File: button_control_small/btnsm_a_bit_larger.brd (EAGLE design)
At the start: 41.4 x 41.4 mm, 63 parts, among them IC2 MEGA8-AI, J1 AVR_SPI_PROG_3X2NS, J2 OUT-, J3 OUT+, Q1 2N2007 (SOT323), Q2 IRLML9301, Q3 IRLML9301, Q4 2N2007 (SOT323), Q5 IRLML9301, T1 BC848, T2 BC848, T3 BC848, T4 BC848, T5 BC848, U1 ACS711ELCTR-25AB-T

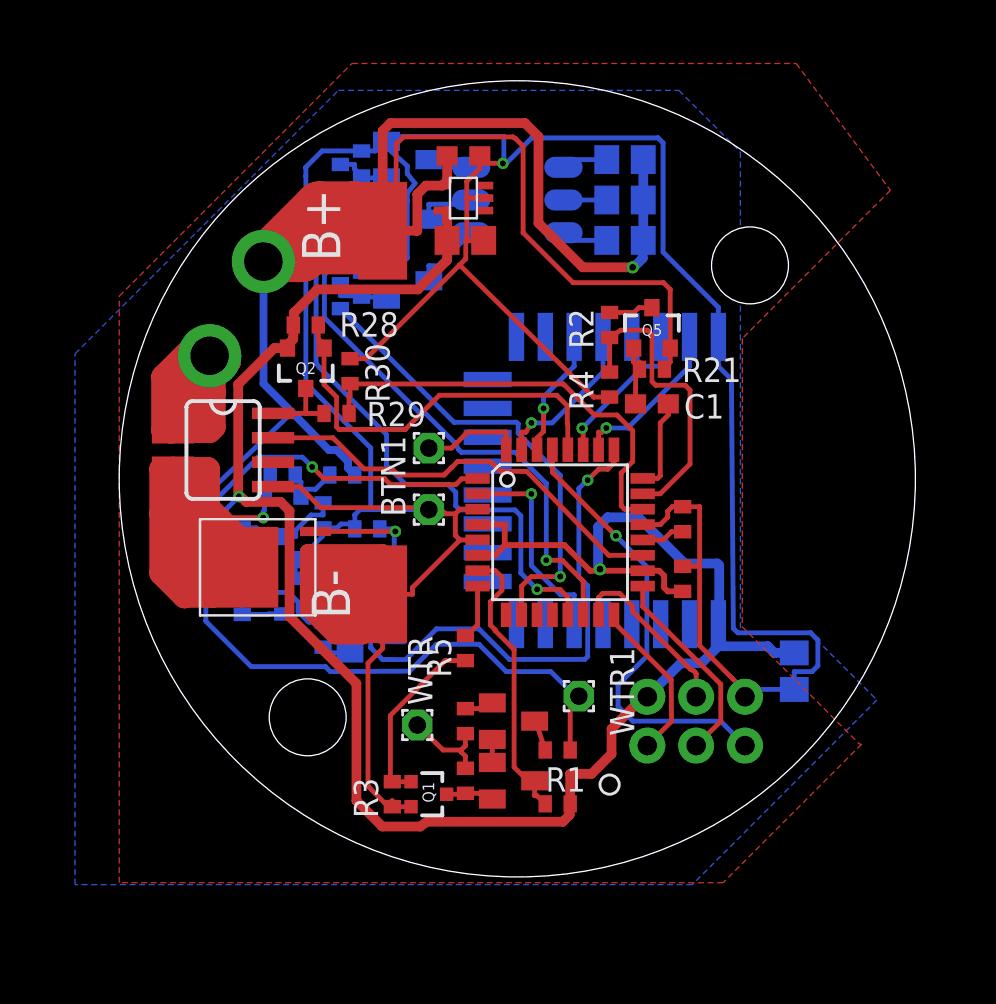
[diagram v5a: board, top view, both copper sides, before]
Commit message: Switched to HC-05
Added protection for water-input
Added separate power supply for BT & DS18B20
Added DS18B20
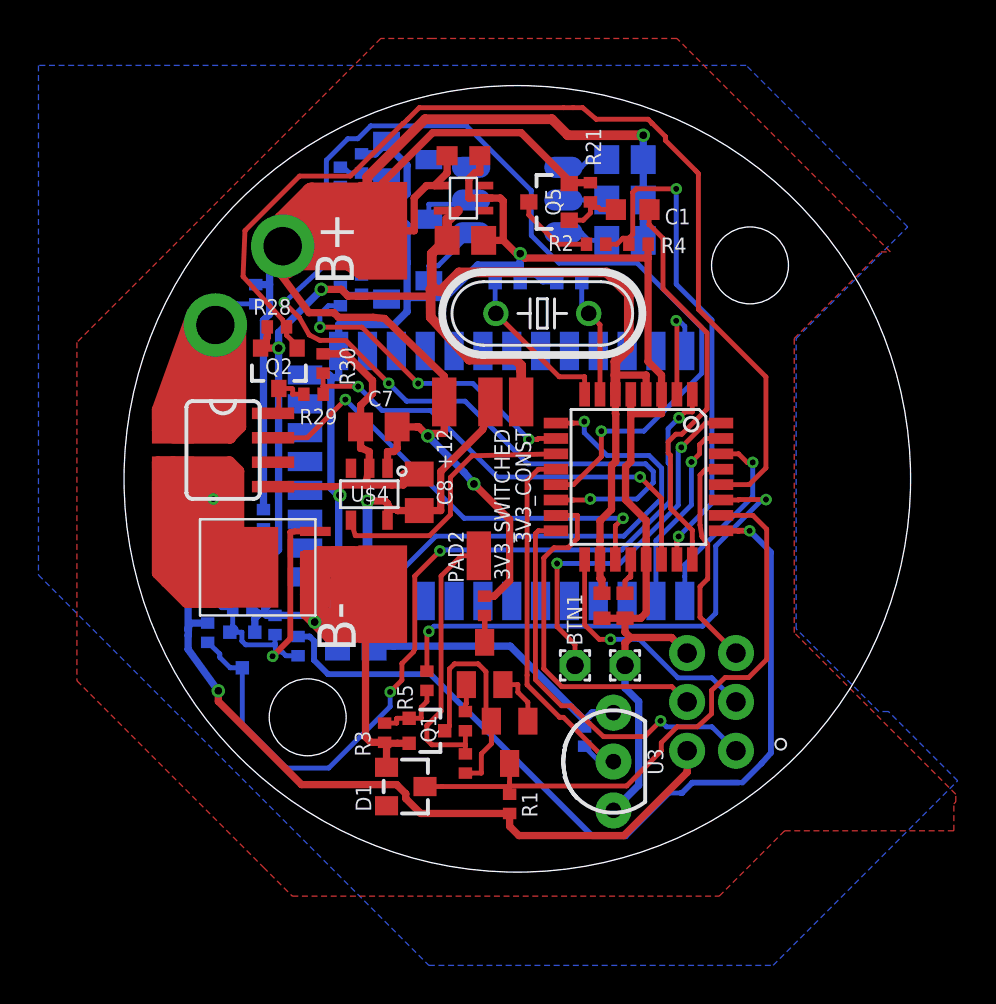
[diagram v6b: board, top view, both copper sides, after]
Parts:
- removed D3: BAT54, diode:SOT23
- removed JDY-08: JDY-08, jdy-08:JDY-08
- removed WTR: WTR-IN, wirepad:1,6/0,9
- removed WTR1: WTR-PWR, wirepad:1,6/0,9
- added +12: +12, wirepad:SMD1,27-2,54
- added 3V3_CONST: 3V_SW, wirepad:SMD1,27-2,54
- added 3V3_SWITCHED: 3V3, wirepad:SMD1,27-2,54
- added C10: 16pF, resistor:C0402
- added C7, C8: 1uF, resistor:C0805
- added C9: 10uF, resistor:C0805
- added PAD2: WTR_IN, wirepad:SMD1,27-2,54
- added Q6: 3.6864MHz, adafruit:HC49/S
- added R31: 4.7k, rcl:R0402
- added U$4: MCP1804, 1804:SOT-23-5
- added U2: HC_05, Bluetooth HC-05:BLUETOOTH_SMD
- added U3: DS18B20, SparkFun-Sensors:TO-92-AMMO
- C1: device resistor:C0603 -> resistor:C0603K
- C6: value 10uF -> 16pF; device resistor:C0805 -> resistor:C0402
- D1: value BAT54 -> BZX84CSMD; device diode:SOT23 -> diode:TO236
- Q1, Q4: value 2N2007 (SOT323) -> 310mA/60V/1.6Ω
- Q2, Q3, Q5: value IRLML9301 -> 4.3A/20V/54mΩ
- R18: value 200 -> 10k
- moved C6 23.4 mm to (22.7, 30.3), turned to 180 degrees
- moved R18 18.0 mm to (6.40, 29.6), turned to 270 degrees
- moved BTN1 13.6 mm to (23.0, 10.3)
- moved BTN2 13.0 mm to (25.6, 10.3)
- moved C1 10.1 mm to (26.0, 34.0)
- moved R21 9.74 mm to (23.8, 34.9), turned to 90 degrees
- moved Q5 8.46 mm to (21.7, 34.4), turned to 90 degrees
- moved R9 8.41 mm to (18.3, 13.4), turned to 90 degrees
- moved D1 8.10 mm to (14.2, 4.00), flipped to the top, turned to 270 degrees
- moved R4 7.45 mm to (26.3, 32.2), turned to 0 degrees
- moved R20 6.93 mm to (7.40, 12.4), turned to 90 degrees
- moved C5 5.41 mm to (25.6, 13.4), turned to 90 degrees
- moved IC2 4.99 mm to (26.3, 20.1), turned to 270 degrees
- moved R15 4.88 mm to (6.50, 14.6), turned to 180 degrees
- moved R27 4.70 mm to (6.80, 17.9), turned to 270 degrees
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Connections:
- net N$1 renamed R+
- net N$12 renamed PD3
- net N$14 renamed PC1
- net N$18 renamed WTR_MEASURE_PULLUP
- net N$21 renamed PC2
- net N$22 renamed PC0
- net N$24 renamed B-
- net N$25 renamed G-
- net N$26 renamed R-
- net N$27 renamed B-BASE
- net N$28 renamed G-BASE
- net N$29 renamed R-BASE
- net N$3 renamed B+
- net N$30 renamed PB2
- net N$31 renamed PB1
- net N$36 renamed PWR_MEASURE_VCC
- net N$5 renamed G+
- net N$6 renamed WTR_MEASURE_ON
- net N$7 renamed GND_OUT_MEASURE
- net PWM0 renamed PD6(PWM0)
- removed net N$10: Q4.1, R16.1, R18.2, R6.1
- removed net N$15: D1.1, R18.1
- removed net N$16: R10.2, R8.1, WTR.1
- removed net N$19: D3.1, R19.1
- removed net N$20: D1.3, D3.3, R20.1, U$1.4
- removed net N$33: IC2.26, JDY-08.23
- removed net N$34: J2.1, U1.1, U1.2
- removed net N$35: IC2.27, JDY-08.22
- removed net N$37: IC2.2, JDY-08.6
- removed net N$38: IC2.30, JDY-08.19
- removed net N$39: IC2.31, JDY-08.20
- new net GND_OUT: J2.1, R18.2, U1.1, U1.2
- new net OUT_BASE: Q4.1, R16.1, R19.1, R20.1, R6.1, U$1.4
- new net PB0: IC2.12, R31.1, U3.2
- new net PC3: D1.C, IC2.26, R1.1, T2.3
- new net PC4: IC2.27, R5.2
- new net PD4-HC05_KEY: IC2.2, U2.34
- new net PD5-HC05_RST: IC2.9, U2.11
- new net PD7: IC2.11, U$4.4
- new net RX(UC): IC2.30, U2.1
- new net TX(UC): IC2.31, U2.2
- new net VCC: 3V3_SWITCHED.1, C8.1, C9.1, R31.2, U$4.5, U2.12, U3.3
- new net WTR-IN: PAD2.1, R10.2, R8.1
- net +12V: now also +12.1, C7.1, R18.1, U$4.1; no longer WTR1.1
- net GND: now also C10.1, C6.1, C7.2, C8.2, C9.2, D1.A, U$4.2, U2.13, U2.21, U2.22, U3.1; no longer C6.2, JDY-08.24
- net PB6: now also C6.2, Q6.2; no longer R1.1, T2.3
- net PB7: now also C10.2, Q6.1; no longer R5.2
- net VDD: now also 3V3_CONST.1; no longer C6.1, JDY-08.1
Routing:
- net GND_OUT: track 0.00 -> 62.5 mm
- net GND_OUT_MEASURE: track 57.5 -> 100.4 mm
- net VCC: track 0.00 -> 33.9 mm, vias 0 -> 1
- net ADC5: track 21.0 -> 54.4 mm
- net PC3: track 0.00 -> 32.5 mm
- net PC4: track 0.00 -> 26.9 mm, vias 0 -> 2
- net GND: track 212.9 -> 186.8 mm, vias 1 -> 3
- net PD5-HC05_RST: track 0.00 -> 25.2 mm, vias 0 -> 1
- net N$34: track 22.6 -> 0.00 mm
- net PB0: track 0.00 -> 20.3 mm
- net PD3: track 24.3 -> 43.9 mm, vias 1 -> 3
- net OUT_BASE: track 0.00 -> 16.5 mm, vias 0 -> 1
- net PC1: track 4.89 -> 21.0 mm
- net WTR-IN: track 0.00 -> 14.5 mm
- net PD7: track 0.00 -> 14.1 mm
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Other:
- board size 41.4 x 41.4 mm -> 40.9 x 40.9 mm

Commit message: Removed extra route, slight changes to ground poly
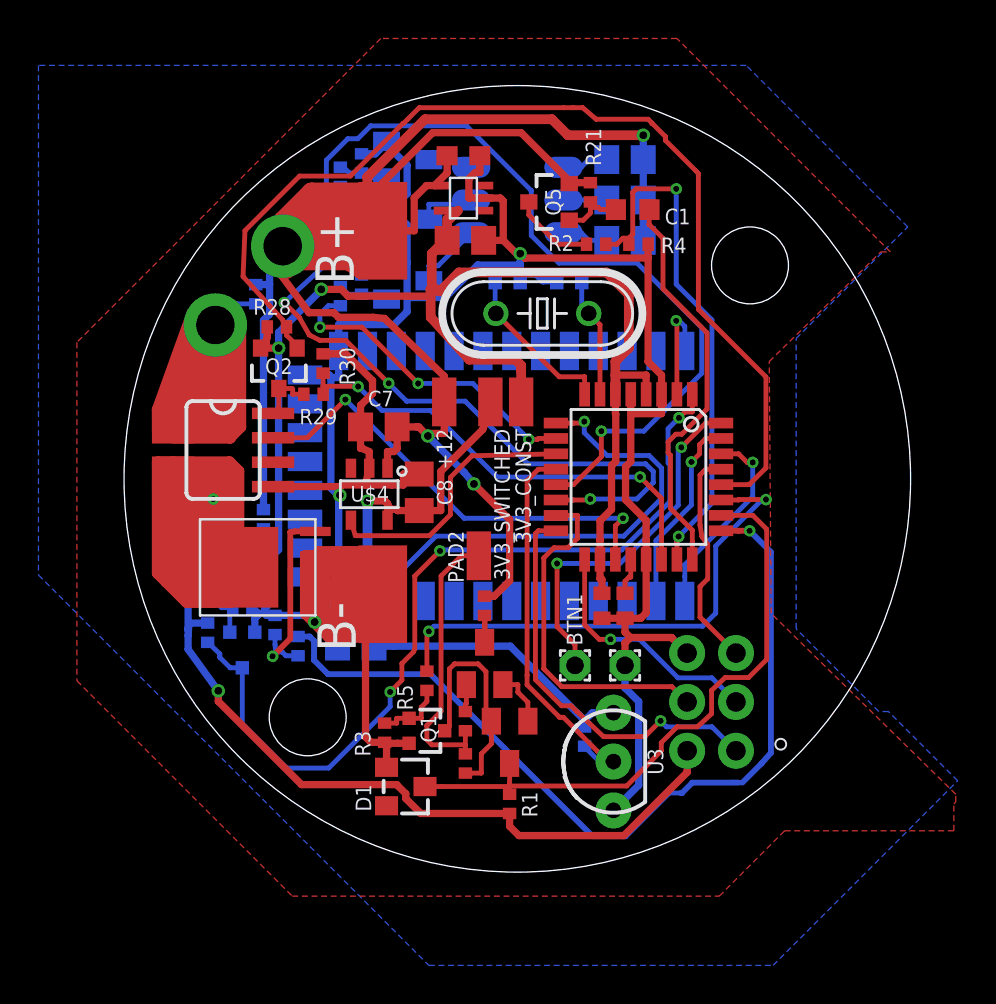
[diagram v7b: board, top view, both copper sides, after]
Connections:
- new net N$1: Q4.1, R16.1, R6.1
- net OUT_BASE: no longer Q4.1, R16.1, R6.1
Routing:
- net OUT_BASE: track 16.5 -> 10.6 mm
- net N$1: track 0.00 -> 3.04 mm
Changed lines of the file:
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@@
 <wire x1="12.2" y1="13.6" x2="12.2" y2="15.3" width="0.6096" layer="1"/>
 <polygon width="0.254" layer="1">
-<vertex x="34.4" y="27.3"/>
+<vertex x="33.1" y="26.1"/>
 <vertex x="38.9" y="31.8"/>
 <vertex x="39.4" y="31.8"/>
 <vertex x="28.3" y="42.9"/>
-<vertex x="15.6" y="42.9"/>
 <vertex x="12.9" y="42.9"/>
 <vertex x="-2.9" y="27.1"/>
 <vertex x="-2.9" y="9.5"/>
-<vertex x="6.8" y="-0.2"/>
 <vertex x="8.3" y="-1.7"/>
 <vertex x="30.5" y="-1.7"/>
@@
 <vertex x="42.8" y="3.2"/>
 <vertex x="42.8" y="3.6"/>
-<vertex x="34.4" y="12"/>
+<vertex x="33.2" y="13"/>
 </polygon>
 <polygon width="0.381" layer="16" isolate="0.2">
@@
 <signal name="OUT_BASE">
 <contactref element="R19" pad="1"/>
-<contactref element="R6" pad="1"/>
-<contactref element="Q4" pad="1"/>
-<contactref element="R16" pad="1"/>
 <contactref element="R20" pad="1"/>
 <contactref element="U$1" pad="4"/>
@@
 <wire x1="7.770609375" y1="10.99998125" x2="7.437359375" y2="10.99998125" width="0.254" layer="16"/>
 <wire x1="8.6" y1="10.8" x2="7.970590625" y2="10.8" width="0.254" layer="16"/>
-<wire x1="7.4" y1="11.45335" x2="7.4" y2="11.36975" width="0.254" layer="16"/>
-<wire x1="7.4" y1="11.36975" x2="5.872440625" y2="11.36975" width="0.254" layer="16"/>
-<wire x1="5.872440625" y1="11.36975" x2="5.679409375" y2="11.56278125" width="0.254" layer="16"/>
-<wire x1="5.679409375" y1="11.56278125" x2="5.679409375" y2="12.025" width="0.254" layer="16"/>
-<wire x1="5.364709375" y1="12.025" x2="5.679409375" y2="12.025" width="0.254" layer="16"/>
 <wire x1="9.5" y1="17.265" x2="8.420590625" y2="17.265" width="0.3048" layer="1"/>
 <via x="7.27528125" y="10.773059375" extent="1-16" drill="0.3048" diameter="0.6096"/>
-<wire x1="7.4" y1="11.9" x2="7.4" y2="11.45335" width="0.254" layer="16"/>
-<wire x1="5.2" y1="13.3" x2="5.2" y2="12.370590625" width="0.254" layer="16"/>
-<wire x1="5.364709375" y1="12.025" x2="5.364709375" y2="12.20588125" width="0.254" layer="16"/>
-<wire x1="5.364709375" y1="12.20588125" x2="5.2" y2="12.370590625" width="0.254" layer="16"/>
-<wire x1="5.05" y1="12.025" x2="5.364709375" y2="12.025" width="0.254" layer="16"/>
-<wire x1="3.6" y1="13.6" x2="4.229409375" y2="13.6" width="0.254" layer="16"/>
-<wire x1="5.2" y1="13.3" x2="4.620590625" y2="13.3" width="0.254" layer="16"/>
-<wire x1="4.229409375" y1="13.6" x2="4.429409375" y2="13.49118125" width="0.254" layer="16"/>
-<wire x1="4.429409375" y1="13.49118125" x2="4.620590625" y2="13.3" width="0.254" layer="16"/>
+<wire x1="7.4" y1="11.9" x2="7.4" y2="11.36975" width="0.254" layer="16"/>
 </signal>
 <signal name="PC2">
@@
 <wire x1="15.3" y1="11.97205" x2="15.4018" y2="12.07025" width="0.254" layer="1"/>
 </signal>
+<signal name="N$1">
+<contactref element="R6" pad="1"/>
+<contactref element="Q4" pad="1"/>
+<contactref element="R16" pad="1"/>
+<wire x1="3.6" y1="13.6" x2="4.229409375" y2="13.6" width="0.254" layer="16"/>
+<wire x1="5.2" y1="13.3" x2="4.620590625" y2="13.3" width="0.254" layer="16"/>
+<wire x1="4.229409375" y1="13.6" x2="4.429409375" y2="13.49118125" width="0.254" layer="16"/>
+<wire x1="4.429409375" y1="13.49118125" x2="4.620590625" y2="13.3" width="0.254" layer="16"/>
+<wire x1="5.2" y1="13.3" x2="5.05" y2="13.15" width="0.254" layer="16"/>
+<wire x1="5.05" y1="13.15" x2="5.05" y2="12.025" width="0.254" layer="16"/>
+</signal>
 </signals>

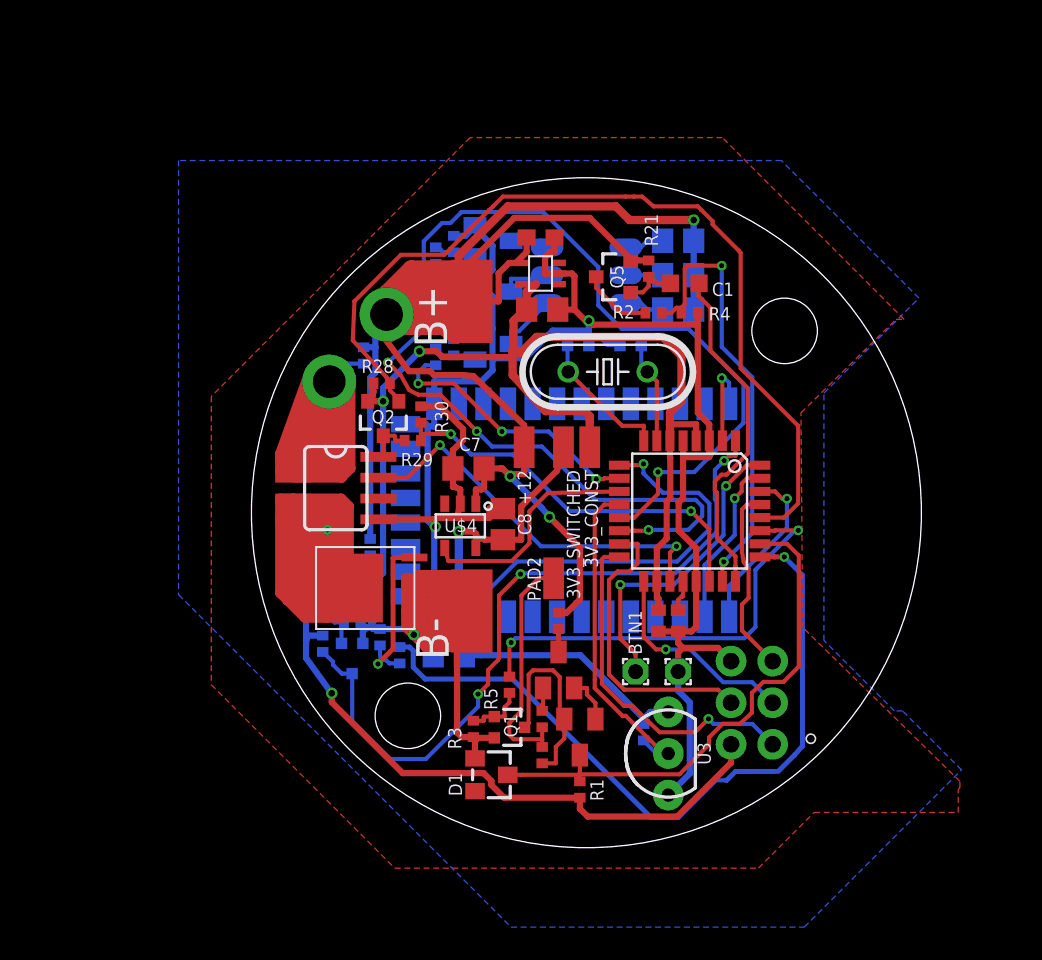
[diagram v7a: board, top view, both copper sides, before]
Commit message: Added FRAM and extra capacitors
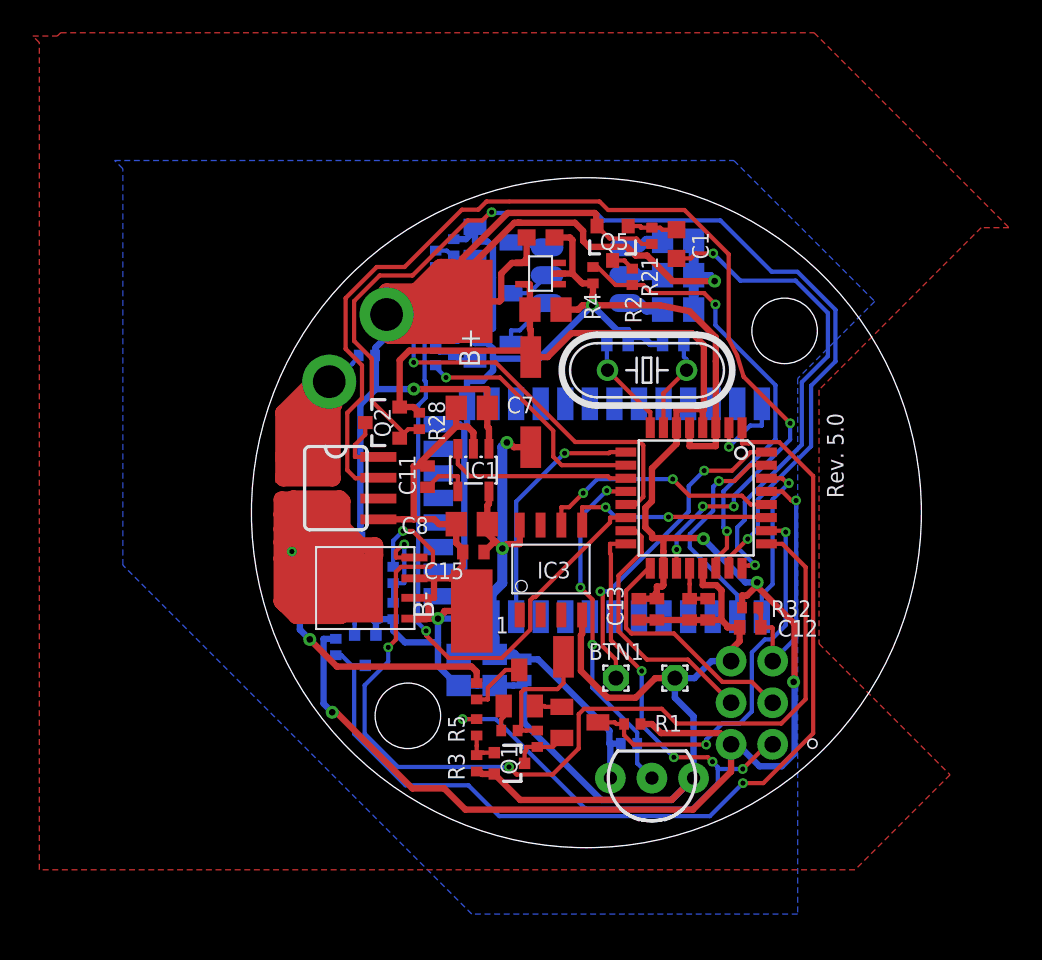
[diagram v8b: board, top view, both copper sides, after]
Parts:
- removed +12: +12, wirepad:SMD1,27-2,54
- removed D1: BZX84CSMD, diode:TO236
- removed R29, R30: 100k, rcl:R0402
- removed U$4: MCP1804, 1804:SOT-23-5
- added C11, C13, C14, C16: 10n, resistor:C0402
- added C12, C15: 100n, resistor:C0402
- added C17: 1uF, resistor:C0805
- added IC1: LP298XS, adafruit:SOT23-5L
- added IC3: FM24-SG, ramtron-2:SO8
- added R32: 10k, rcl:R0402
- moved R9 6.59 mm to (13.3, 9.10)
- moved 3V3_CONST 6.57 mm to (16.6, 29.5)
- moved R4 6.33 mm to (20.4, 34.5), turned to 270 degrees
- moved R1 5.12 mm to (22.8, 7.10), turned to 0 degrees
- moved R19 4.92 mm to (8.20, 16.2)
- moved PAD2 4.84 mm to (18.6, 11.2), turned to 0 degrees
- moved C7 3.71 mm to (13.0, 26.4)
- moved R5 3.28 mm to (13.3, 6.90)
- moved R28 3.25 mm to (9.80, 25.6), turned to 90 degrees
- moved T1 2.64 mm to (15.9, 9.30)
- moved C6 2.60 mm to (25.3, 30.3)
- moved R2 2.56 mm to (22.8, 34.4), turned to 270 degrees
- moved C1 2.45 mm to (25.5, 36.4), turned to 90 degrees
- moved Q6 2.40 mm to (23.7, 28.7)
- moved C10 2.40 mm to (21.9, 30.3)
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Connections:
- removed net ADC5: IC2.28, Q2.1, R28.1
- removed net MISO: IC2.16, J1.1
- removed net PC4: IC2.27, R5.2
- new net N$2: C11.1, IC1.4
- new net PB4/MISO: IC2.16, J1.1, R5.2
- new net SCL: IC2.28, IC3.6
- new net SDA: IC2.27, IC3.5
- net +12V: now also IC1.1; no longer +12.1, U$4.1
- net ADC7: now also R2.2, R4.1; no longer R29.2, R30.1
- net AREF: now also C14.1
- net GND: now also C11.2, C12.2, C13.2, C14.2, C15.2, C16.2, C17.2, IC1.2, IC3.4; no longer D1.A, R30.2, U$4.2
- net PC0: now also Q2.1, R28.1; no longer R2.2, R4.1
- net PC3: no longer D1.C
- net PD7: now also IC1.3; no longer U$4.4
- net PWR_MEASURE_VCC: no longer R29.1
- net RST: now also C12.1, R32.1
- net VCC: now also C15.1, C16.1, C17.1, IC1.5, IC3.8; no longer U$4.5
- net VDD: now also C13.1, R32.2
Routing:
- net ADC5: track 54.4 -> 0.00 mm
- net PB4/MISO: track 0.00 -> 42.8 mm, vias 0 -> 5
- net ADC6: track 23.9 -> 65.1 mm, vias 2 -> 4
- net PC0: track 27.2 -> 63.4 mm
- net PC4: track 26.9 -> 0.00 mm, vias 2 -> 0
- net GND_OUT_MEASURE: track 100.4 -> 76.7 mm
- net GND_OUT: track 62.5 -> 39.9 mm
- net MISO: track 21.3 -> 0.00 mm, vias 1 -> 0
- net PC2: track 44.9 -> 61.5 mm, vias 1 -> 3
- net PD3: track 43.9 -> 60.3 mm, vias 3 -> 1
- net SCL: track 0.00 -> 15.0 mm, vias 0 -> 2
- net PB1: track 41.2 -> 26.9 mm
- net SDA: track 0.00 -> 12.8 mm, vias 0 -> 2
- net PD5-HC05_RST: track 25.2 -> 15.0 mm
- net PC1: track 21.0 -> 30.0 mm, vias 0 -> 2
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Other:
- board text added: "Rev. 5.0"
